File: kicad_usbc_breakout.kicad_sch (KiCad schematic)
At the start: 6 parts, among them J1 USB_C_Receptacle_USB2.0_16P, J2 Conn_01x01

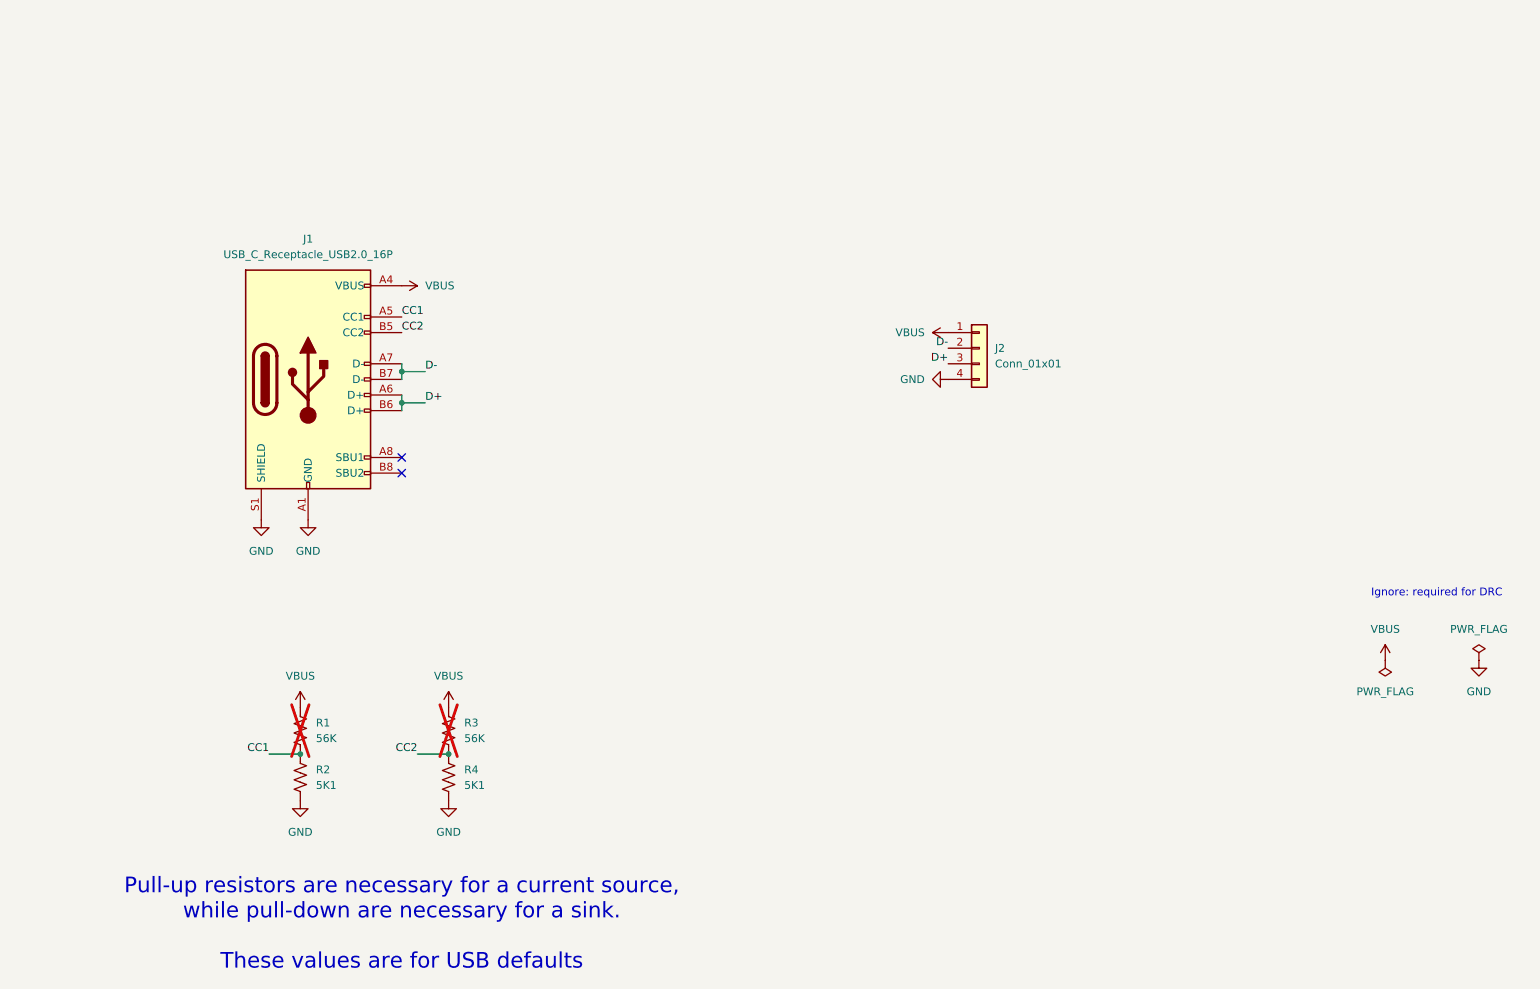
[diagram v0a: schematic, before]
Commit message: initial pcb placement
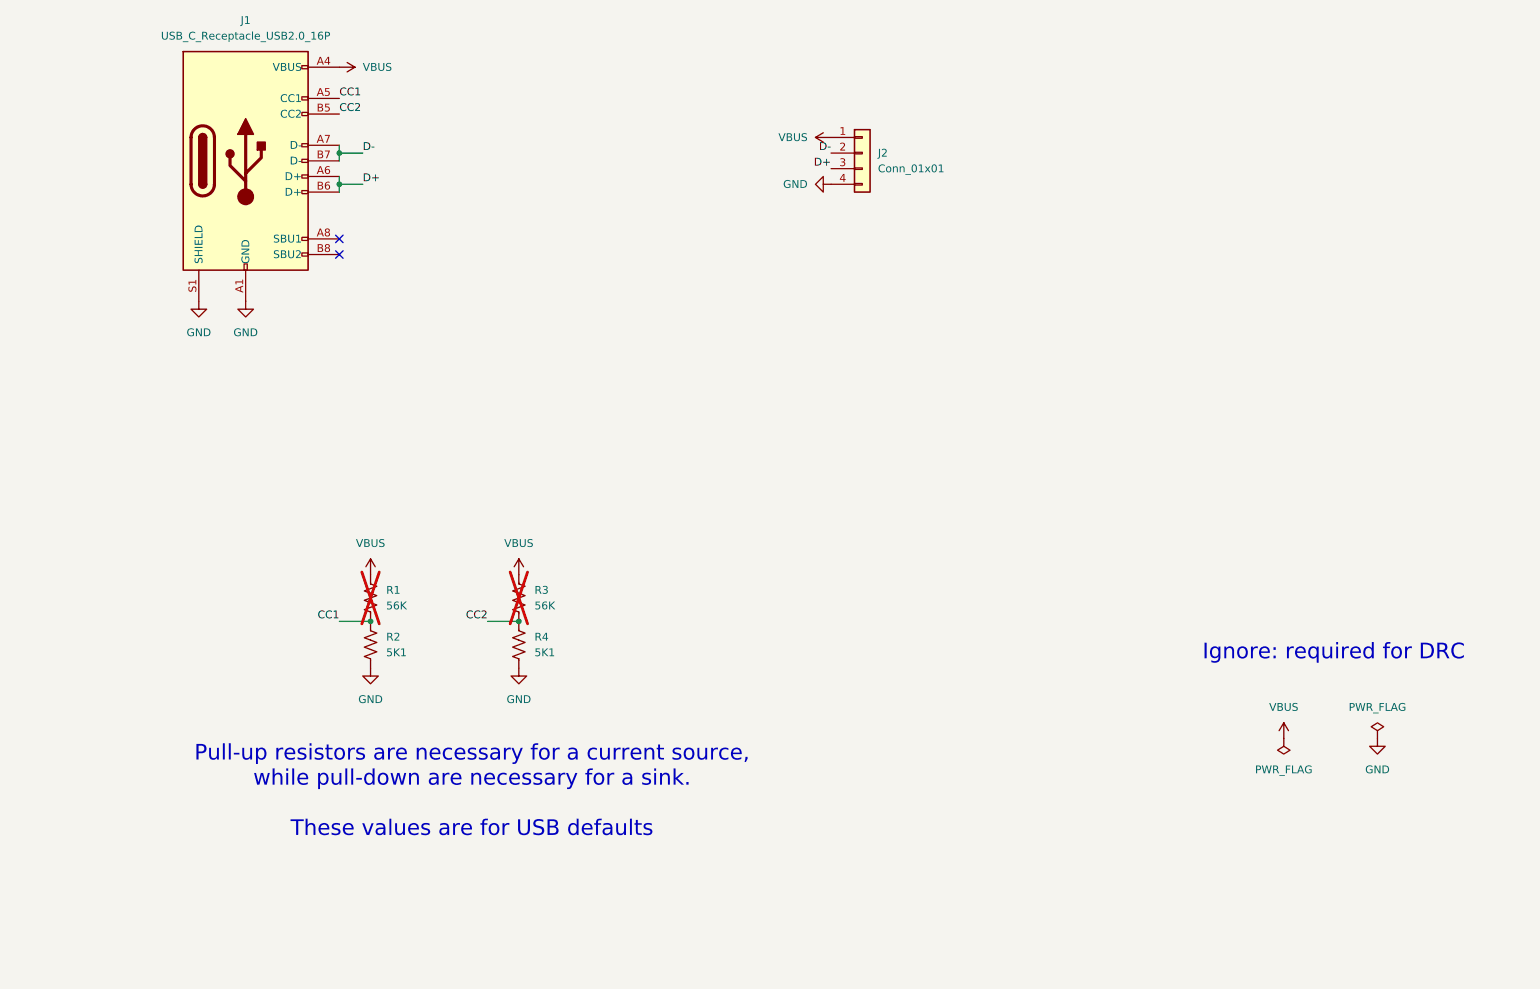
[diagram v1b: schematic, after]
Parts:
- J1: MFR (none) -> GCT; MFR Part Num (none) -> USB4085-GF-A
- R1, R3: MFR (none) -> Vishay; MFR Part Num (none) -> CRCW120656K0FKEA
- R2, R4: MFR (none) -> Vishay; MFR Part Num (none) -> CRCW12065K10FKEA
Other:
- moved on the sheet: J1, J2, R1, R2, R3, R4

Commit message: re-placed and routed to make more compact
also changed to 0805 resistors
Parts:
- J2: footprint Connector_Wire:SolderWire-0.5sqmm_1x04_P4.8mm_D0.9mm_OD2.3mm_Relief2x -> Connector_Wire:SolderWire-0.5sqmm_1x04_P4.8mm_D0.9mm_OD2.3mm_Relief
- R1, R3: footprint Resistor_SMD:R_1206_3216Metric_Pad1.30x1.75mm_HandSolder -> Resistor_SMD:R_0805_2012Metric_Pad1.20x1.40mm_HandSolder; MFR Part Num CRCW120656K0FKEA -> CRCW080556K0FKEA
- R2, R4: footprint Resistor_SMD:R_1206_3216Metric_Pad1.30x1.75mm_HandSolder -> Resistor_SMD:R_0805_2012Metric_Pad1.20x1.40mm_HandSolder; MFR Part Num CRCW12065K10FKEA -> CRCW08055K10FKEA
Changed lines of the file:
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@@
 			)
 		)
-		(property "Footprint" "Resistor_SMD:R_1206_3216Metric_Pad1.30x1.75mm_HandSolder"
+		(property "Footprint" "Resistor_SMD:R_0805_2012Metric_Pad1.20x1.40mm_HandSolder"
 			(at 97.536 133.604 90)
 			(effects
@@
 			)
 		)
-		(property "MFR Part Num" "CRCW12065K10FKEA"
+		(property "MFR Part Num" "CRCW08055K10FKEA"
 			(at 96.52 133.35 0)
 			(effects
@@
 			)
 		)
-		(property "Footprint" "Resistor_SMD:R_1206_3216Metric_Pad1.30x1.75mm_HandSolder"
+		(property "Footprint" "Resistor_SMD:R_0805_2012Metric_Pad1.20x1.40mm_HandSolder"
 			(at 73.406 125.984 90)
 			(effects
@@
 			)
 		)
-		(property "MFR Part Num" "CRCW120656K0FKEA"
+		(property "MFR Part Num" "CRCW080556K0FKEA"
 			(at 72.39 125.73 0)
 			(effects
@@
 			)
 		)
-		(property "Footprint" "Resistor_SMD:R_1206_3216Metric_Pad1.30x1.75mm_HandSolder"
+		(property "Footprint" "Resistor_SMD:R_0805_2012Metric_Pad1.20x1.40mm_HandSolder"
 			(at 73.406 133.604 90)
 			(effects
@@
 			)
 		)
-		(property "MFR Part Num" "CRCW12065K10FKEA"
+		(property "MFR Part Num" "CRCW08055K10FKEA"
 			(at 72.39 133.35 0)
 			(effects
@@
 			)
 		)
-		(property "Footprint" "Resistor_SMD:R_1206_3216Metric_Pad1.30x1.75mm_HandSolder"
+		(property "Footprint" "Resistor_SMD:R_0805_2012Metric_Pad1.20x1.40mm_HandSolder"
 			(at 97.536 125.984 90)
 			(effects
@@
 			)
 		)
-		(property "MFR Part Num" "CRCW120656K0FKEA"
+		(property "MFR Part Num" "CRCW080556K0FKEA"
 			(at 96.52 125.73 0)
 			(effects
@@
 			)
 		)
-		(property "Footprint" "Connector_Wire:SolderWire-0.5sqmm_1x04_P4.8mm_D0.9mm_OD2.3mm_Relief2x"
+		(property "Footprint" "Connector_Wire:SolderWire-0.5sqmm_1x04_P4.8mm_D0.9mm_OD2.3mm_Relief"
 			(at 152.4 53.34 0)
 			(effects

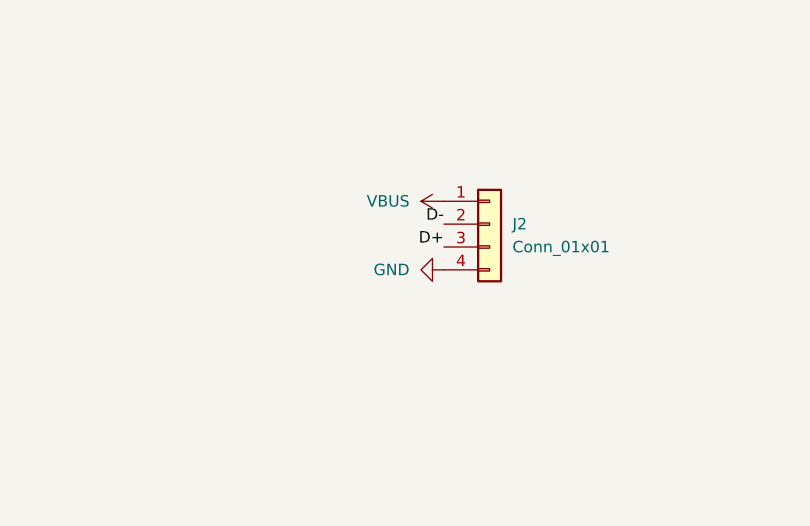
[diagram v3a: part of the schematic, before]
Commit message: switched around wires so that gnd and vbus are next to eachother
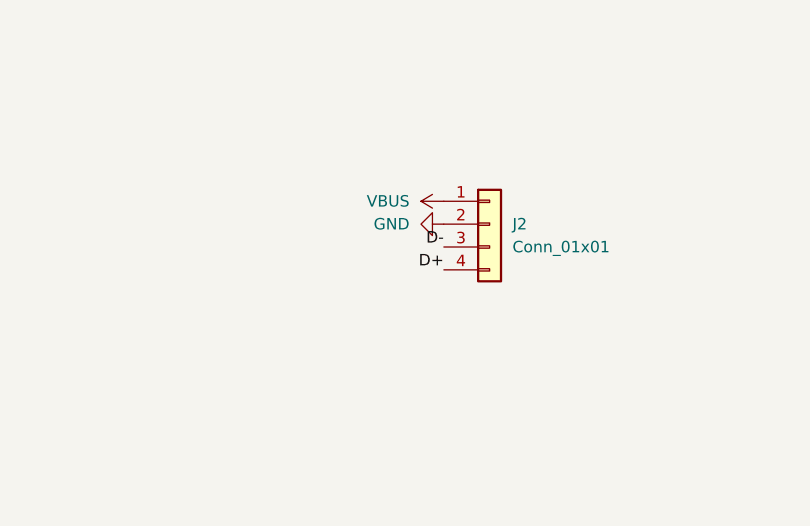
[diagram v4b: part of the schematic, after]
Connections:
- net D+: now also J2.4 (Pin_4); no longer J2.3 (Pin_3)
- net D-: now also J2.3 (Pin_3); no longer J2.2 (Pin_2)
- net GND: now also J2.2 (Pin_2); no longer J2.4 (Pin_4)
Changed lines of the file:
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@@
 	(title_block
 		(title "USB-C Breakout")
-		(date "2024-03-29")
-		(rev "1.0")
+		(date "2024-03-30")
+		(rev "1.1")
 		(company "HugonLabs")
 		(comment 1 "USB-C connector to wires, with CC resistors")
@@
 	)
 	(label "D+"
-		(at 147.32 55.88 180)
+		(at 147.32 58.42 180)
 		(fields_autoplaced yes)
 		(effects
@@
 	)
 	(label "D-"
-		(at 147.32 53.34 180)
+		(at 147.32 55.88 180)
 		(fields_autoplaced yes)
 		(effects
@@
 	(symbol
 		(lib_id "power:GND")
-		(at 147.32 58.42 270)
+		(at 147.32 53.34 270)
 		(unit 1)
 		(exclude_from_sim no)
@@
 		(fields_autoplaced yes)
 		(property "Reference" "#PWR09"
-			(at 140.97 58.42 0)
+			(at 140.97 53.34 0)
 			(effects
 				(font
@@
 		)
 		(property "Value" "GND"
-			(at 143.51 58.4199 90)
+			(at 143.51 53.3399 90)
 			(effects
 				(font
@@
 		)
 		(property "Footprint" ""
-			(at 147.32 58.42 0)
+			(at 147.32 53.34 0)
 			(effects
 				(font
@@
 		)
 		(property "Datasheet" ""
-			(at 147.32 58.42 0)
+			(at 147.32 53.34 0)
 			(effects
 				(font
@@
 		)
 		(property "Description" "Power symbol creates a global label with name \"GND\" , ground"
-			(at 147.32 58.42 0)
-			(effects
-				(font
+			(at 147.32 53.34 0)
+			(effects
+				(font
